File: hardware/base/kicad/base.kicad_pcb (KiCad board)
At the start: 4 copper layers, 150 x 107.5 mm, 518 parts, among them J1 POWER, J10 LOCAL BUS, J11 SPINDLE A, J12 SPINDLE B, J13 MODBUS, J14 ESTOP | PROBE, J2 USB micro-B, J3 HY911105AE IN, J4 HY911105AE OUT, J5 TC2030, J6 HC-WK88-H132-1X2-55B, J7 HC-WK88-H132-1X2-55B, J8 HC-WK88-H132-1X2-55B, J9 HC-WK88-H132-1X2-55B, Q1 AO3422, Q11 AO3401A, Q2 AO3422, Q3 AO3422, Q4 AO3422, Q5 SS8550, Q6 AO3422, Q7 AO3422, SW1 BOOT, SW2 TERM A B Z, SW3 TERM A B Z, SW4 TERM A B Z, SW5 TERM A B Z, U1 TPS54360BDDAR, U10 TPS1H000AQDGNRQ1, U11 ST26C31BDR, U12 LTV-357T-C, U13 TPD4E05U06DQAR, U14 LTV-357T-C, U15 TPD4E05U06DQAR, U16 ST26C31BDR, U17 LTV-357T-C, U18 TPD4E05U06DQAR, U19 LTV-357T-C, U2 TPD4E05U06DQAR, U20 TPD4E05U06DQAR, U21 TPS1H000AQDGNRQ1, U22 AM26LV32EIDR, U23 TPS1H000AQDGNRQ1, U24 AM26LV32EIDR, U25 TPS1H000AQDGNRQ1, U26 AM26LV32EIDR, U27 TPS1H000AQDGNRQ1, U28 AM26LV32EIDR, U29 TLP2361, U3 TPS62A02ADRLR, U30 TPS2553DBVR, U31 TPD4E05U06DQAR, U32 TPD4E05U06DQAR, U33 TPD4E05U06DQAR, U34 TPD4E05U06DQAR, U35 TPD4E05U06DQAR, U36 OPA2990IDR, U37 SN74AHCT1G125DBVR, U38 CA-IS3092W, U39 LTV-357T-C, U4 LAN9253-I/R4X, U40 TPS3828-33DBVR, U5 TPS3808G33DBVR, U6 M24C16-RMN6TP, U7 TPD4E05U06DQAR, U8 TPD4E05U06DQAR, U9 STM32H523VET6, X1 SiT8008BI-71-33E-25.000000

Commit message: Route in stages: ground fanout by script, minimum widths and clearances
- Net classes at the JLCPCB multilayer minimum at no extra cost: 0.1/0.1 mm,
  0.4/0.2 mm vias; buck nodes in a class of their own; board minimums to match.
- route.py works in passes, each from the stage written by the one before
  (kicad/stages/, not versioned); "back" restores a stage.
- Pass "gnd": a stub and a via of its own from every surface pad of GND and
  GNDISO to the layer 2 plane, checked against clearances, holes and planes.
- Modbus placement: bus side parts below the axis of U38, so the GND/GNDISO
  split follows the isolation barrier.
- Fixes: zone outline freed by Python, Zones() after Remove, Freerouting 2.4.1
  needs Java 25 (JAVA variable).
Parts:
- moved R38 26.3 mm to (26.0, 61.9), turned to 0 degrees
- moved D8 25.5 mm to (19.0, 82.5), turned to 0 degrees
- moved R200 25.4 mm to (15.4, 81.1)
- moved C24 25.3 mm to (43.0, 59.7), turned to 90 degrees
- moved C12 24.3 mm to (43.0, 83.2)
- moved R34 22.8 mm to (29.1, 63.5), turned to 0 degrees
- moved C17 22.2 mm to (35.2, 85.2), turned to -90 degrees
- moved R246 21.3 mm to (68.2, 86.2), turned to 0 degrees
- moved R243 16.0 mm to (47.8, 86.4), turned to 0 degrees
- moved R24 14.0 mm to (42.9, 66.7), turned to 90 degrees
- moved C85 13.9 mm to (63.8, 88.7), turned to 180 degrees
- moved C31 12.0 mm to (27.8, 56.2), turned to 90 degrees
- moved JP5 11.4 mm to (53.6, 92.9), turned to 90 degrees
- moved D62 10.3 mm to (79.3, 77.1)
- moved R18 9.84 mm to (38.4, 66.7), turned to 90 degrees
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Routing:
- net GND: track 0.00 -> 214.2 mm, vias 0 -> 301
- net GNDISO: track 0.00 -> 5.60 mm, vias 0 -> 8
- added copper zone on In2.Cu, net +3V3
- added copper zone on In2.Cu, net +5V
- added copper zone on In2.Cu, net +VIN
- added copper zone on B.Cu, net CHASSIS
- added copper zone on In1.Cu, net GND
- added copper zone on In1.Cu, net GNDISO

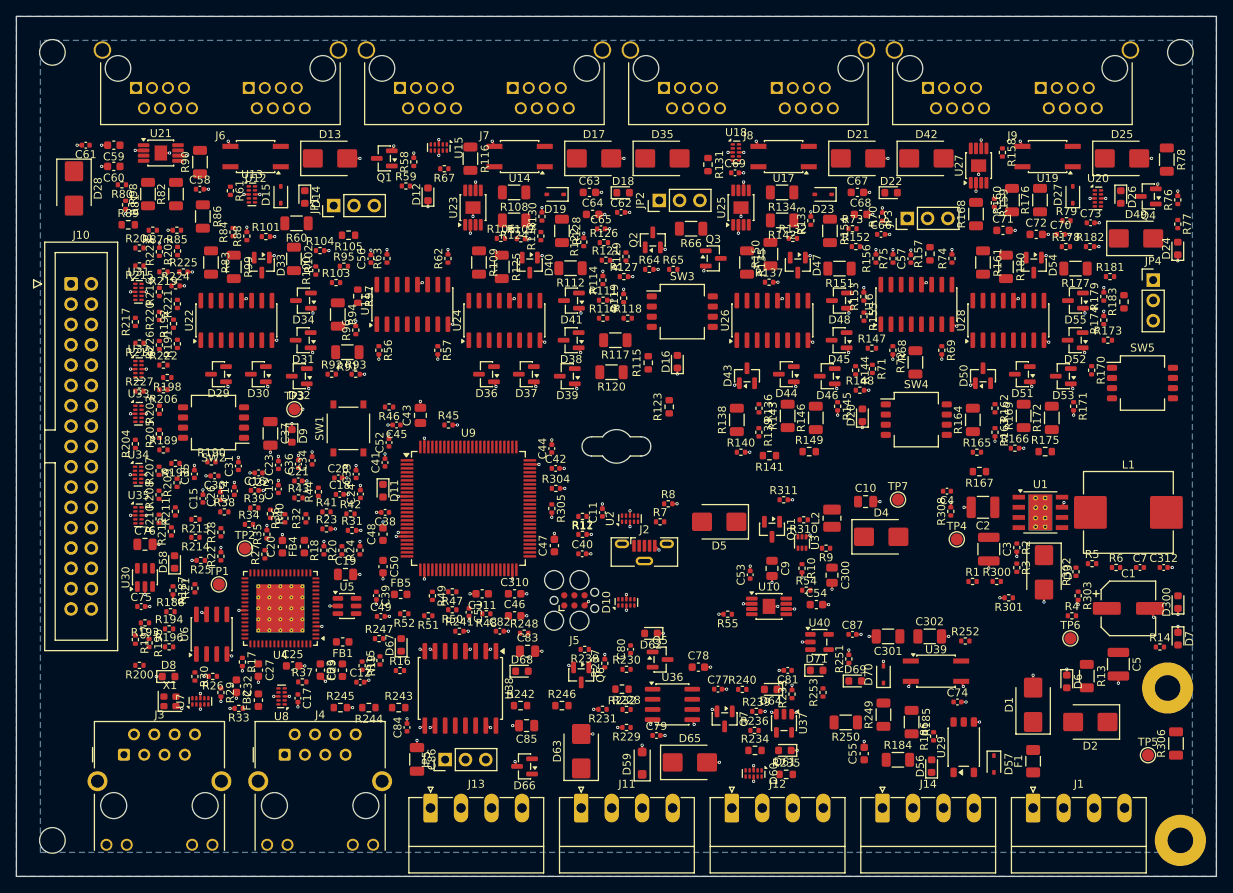
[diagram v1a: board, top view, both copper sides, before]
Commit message: Supply passes one at a time; 3.3 V fanout and layer 4 links
- Passes 3v3, 5v, vin in turn. A pad off its plane gets its via anyway, then a
  layer 4 track, L-shaped first, to a via of the net in its plane (existing or
  new); the linked vias serve the next ones.
- Clearance checks gathered in Copper: pads, tracks and vias of the passes
  before, per layer, holes, planes.
- Layer 3 outlines follow the regulators: +5V down to L1 and C5, +3V3 over the
  3.3 V buck and the safety and drive supply logic, +VIN around the 5 V buck
  input and the power entry.
- C5 against the output of L1, C1 2 mm lower.
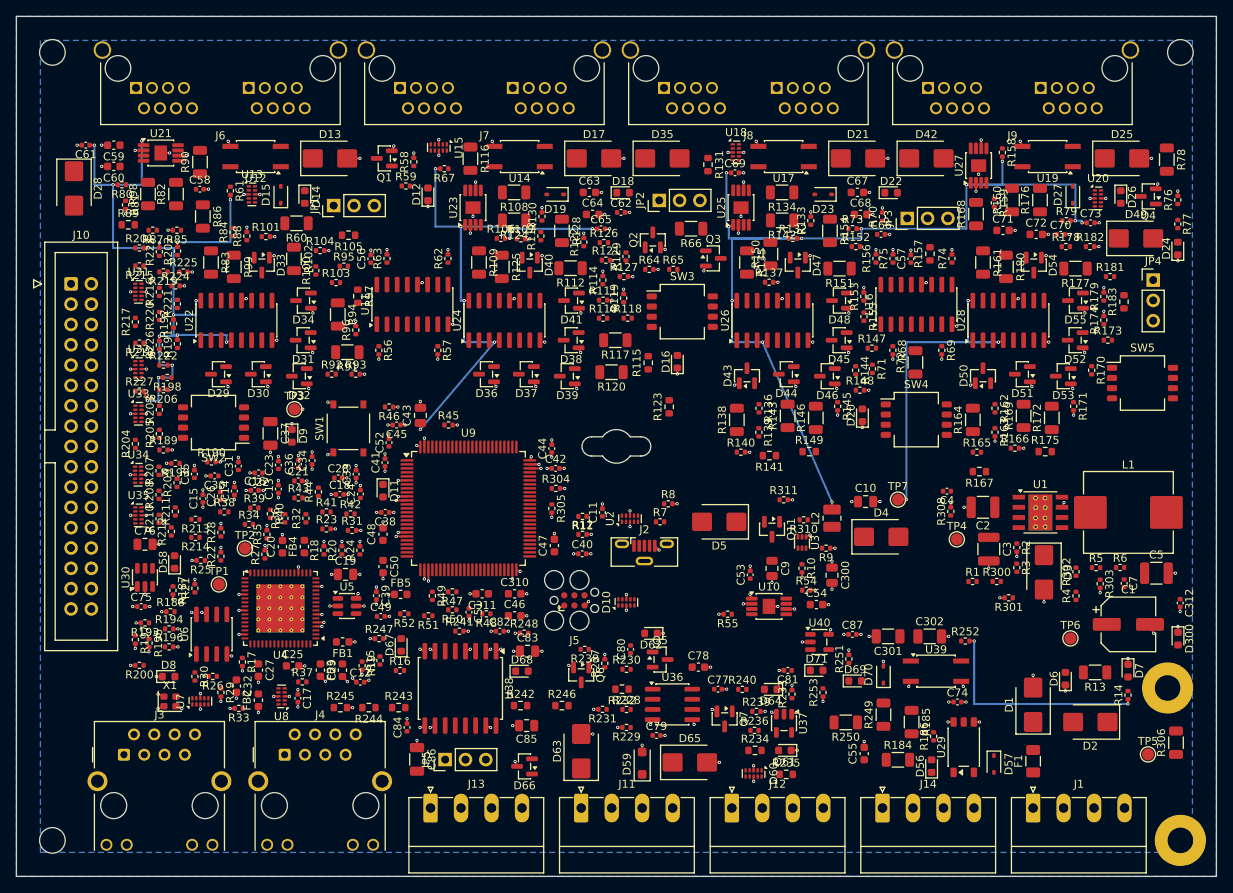
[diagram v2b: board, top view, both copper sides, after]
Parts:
- moved C5 12.3 mm to (142.5, 69.6), turned to 0 degrees
- moved D7 7.42 mm to (138.9, 81.8)
- moved R14 7.21 mm to (138.9, 84.8), turned to 90 degrees
- moved C312 4.89 mm to (145.5, 73.3), turned to -90 degrees
- moved D300 4.57 mm to (145.2, 77.8), turned to -90 degrees
- moved R303 3.13 mm to (135.5, 70.9)
- moved C7 2.80 mm to (138.5, 70.9), turned to -90 degrees
- moved R4 2.54 mm to (132.4, 72.4), turned to 90 degrees
- moved C1 2.00 mm to (139.0, 76.0)
- moved R13 1.14 mm to (134.8, 82.0), turned to 180 degrees
- moved R5 0.71 mm to (135.0, 68.9)
- moved R6 0.50 mm to (138.0, 68.9)
- moved D6 0.39 mm to (131.1, 82.8), turned to 90 degrees
- moved R306 0.10 mm to (144.9, 90.8)
- moved TP5 0.10 mm to (141.4, 92.2)
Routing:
- net +3V3: track 0.00 -> 411.4 mm, vias 0 -> 113

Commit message: Decoupling capacitors against their pins; 3.3 V plane under the axes
- Placement: the ICs and their decoupling capacitors first, each capacitor
  waiting for every IC of its sheet on its supply and kept against the pin, no
  spreading; the other passives after. 27 capacitors were over 3 mm from their
  pin (the ESC ones up to 14 mm), 8 are now, among them C1 placed by hand.
- Modbus bus side: no growth beyond its zone, 3 mm wider into the spindle
  block; JP5 and D66 placed by hand between U38 and J13.
- Layer 3: +3V3 up to y = 47.5 across x = 3 to 131, +5V fed to the axes along
  the right edge.
- Layer 4 links: an existing via of the plane or a new one, whichever gives
  the shorter track (274 mm in all for +3V3, was 335).
- Vias of different nets 1 mm apart: closer, the plane between them is cut and
  a via loses its plane.
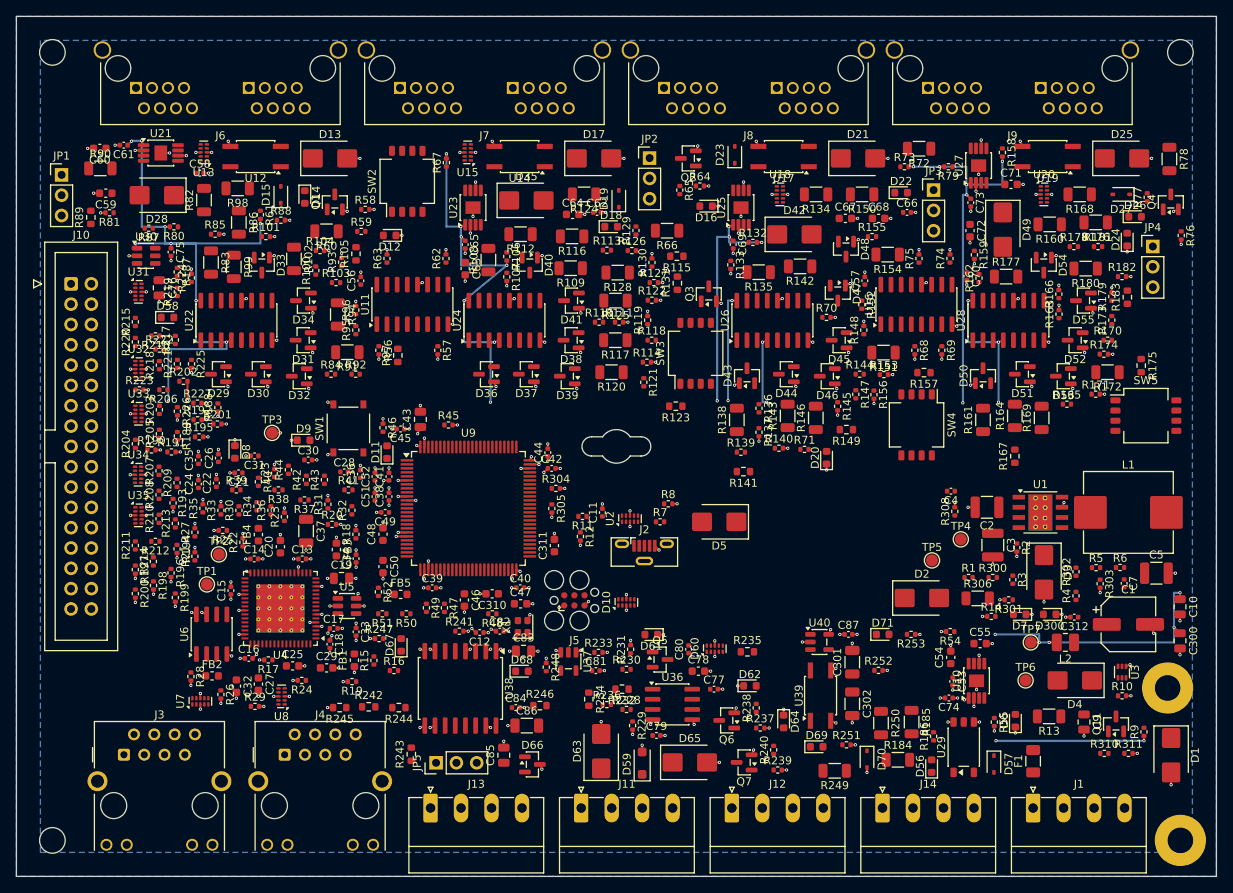
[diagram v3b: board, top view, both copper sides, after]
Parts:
- moved R311 53.5 mm to (139.0, 92.1)
- moved Q11 49.4 mm to (137.4, 88.4), turned to 90 degrees
- moved R310 47.6 mm to (136.0, 92.1), turned to 0 degrees
- moved R9 45.9 mm to (140.9, 89.4), turned to 90 degrees
- moved X1 45.1 mm to (63.3, 76.3), turned to 90 degrees
- moved C75 44.5 mm to (19.3, 29.5), turned to -90 degrees
- moved C300 44.3 mm to (145.4, 78.0)
- moved C9 43.5 mm to (133.4, 88.2)
- moved U3 43.2 mm to (138.2, 82.0)
- moved R10 43.1 mm to (138.2, 84.9), turned to 0 degrees
- moved C10 41.4 mm to (145.4, 73.8), turned to -90 degrees
- moved U30 40.2 mm to (16.2, 29.9), turned to 0 degrees
- moved R187 39.8 mm to (20.1, 31.9)
- moved SW2 38.7 mm to (48.9, 20.6), turned to 90 degrees
- moved TP5 36.3 mm to (114.5, 68.0)
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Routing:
- net +3V3: track 411.4 -> 351.1 mm, vias 113 -> 122
